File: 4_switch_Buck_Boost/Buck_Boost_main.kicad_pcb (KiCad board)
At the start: 4 copper layers, 95 parts, among them J1 Conn_02x02_Counter_Clockwise, J2 Screw_Terminal_2x5.08, J3 Screw_Terminal_2x2.54, J4 Screw_Terminal_2x5.08, Q101 2N7002K, Q102 NVMFS6H836NLT1G, Q103 BSS83P, Q104 BSC070N10LS5, Q105 BSC070N10LS5, Q106 BSC070N10LS5, Q107 BSC070N10LS5, U1 LT8390EUFD_PBF, U101 LTC4372CMS8-PBF

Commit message: Add LT8390EFE#PBF footprint
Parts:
- removed U1: LT8390EUFD_PBF, LT:QFN50P500X400X80-29N
- added U102: LT8390EFE_PBF, LT:05-08-1663_ADI, F.Cu at (144.7, 104.8)
- moved H2 45.8 mm to (207.2, 75.7)
- moved H3 43.9 mm to (87.0, 135.8)
- moved H4 42.6 mm to (201.1, 129.5)
- moved H1 37.8 mm to (87.8, 80.9)
- moved C8 8.31 mm to (152.8, 111.0)
- moved R118 6.16 mm to (134.6, 108.3)
- moved C9 4.58 mm to (136.7, 105.0)
- moved C103 1.86 mm to (145.5, 95.3)
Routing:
- net SW1: track 24.8 -> 6.03 mm
- net ENABLE: track 41.5 -> 24.7 mm
- net SW2: track 20.7 -> 7.21 mm
- net BG1_CTRL: track 11.6 -> 0.00 mm
- net EN/UVLO: track 11.6 -> 0.49 mm
- net Net-(U102-~{PGOOD}): track 9.25 -> 0.04 mm
- net TG1_CTRL: track 7.43 -> 0.00 mm
- net FB: track 25.9 -> 18.9 mm
- net TG2_CTRL: track 6.75 -> 0.00 mm
- net Vout: track 26.5 -> 19.8 mm
- net BG2_CTRL: track 6.33 -> 0.00 mm
- net /Vref: track 6.13 -> 0.00 mm
- net Net-(U102-RT): track 12.9 -> 7.66 mm
- net Net-(U102-SS): track 3.61 -> 0.00 mm
- net Net-(U102-VC): track 3.92 -> 0.52 mm
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
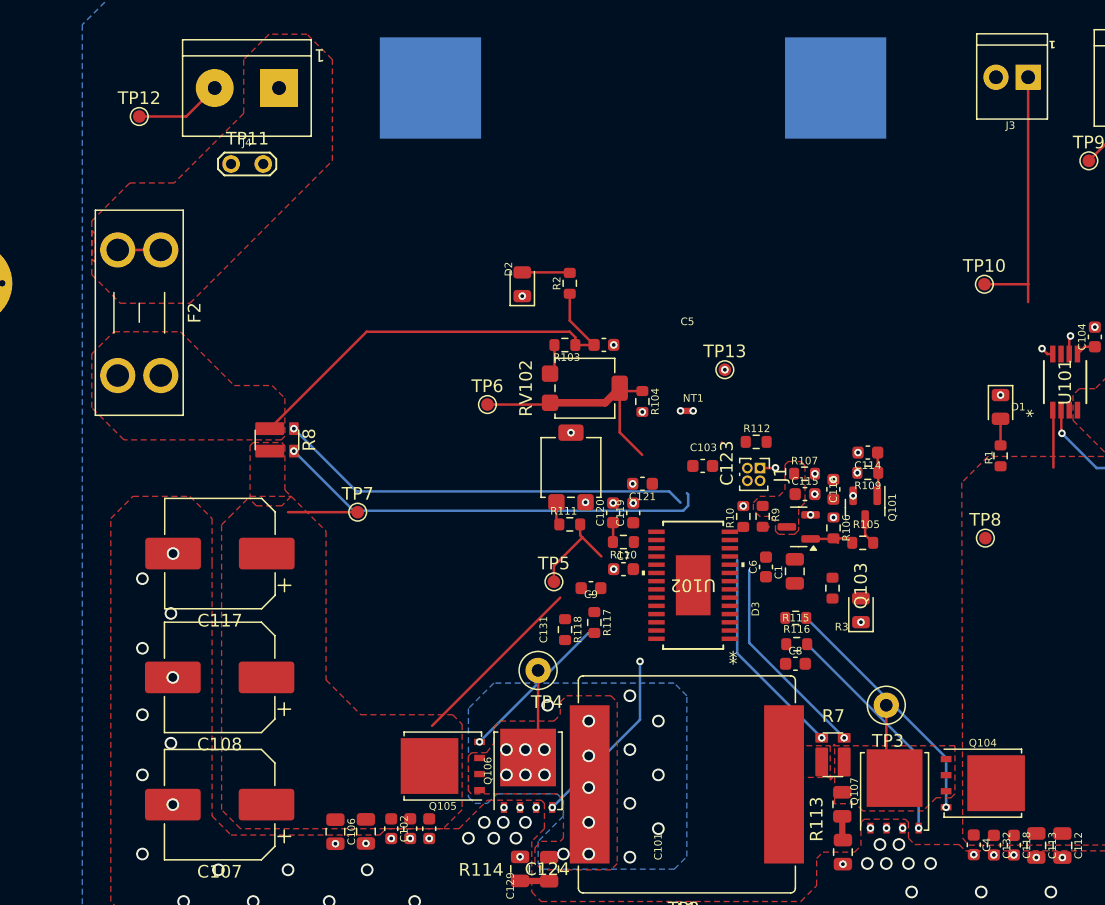
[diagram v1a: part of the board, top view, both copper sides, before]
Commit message: Reconfigured All Analog traces and GNDA island
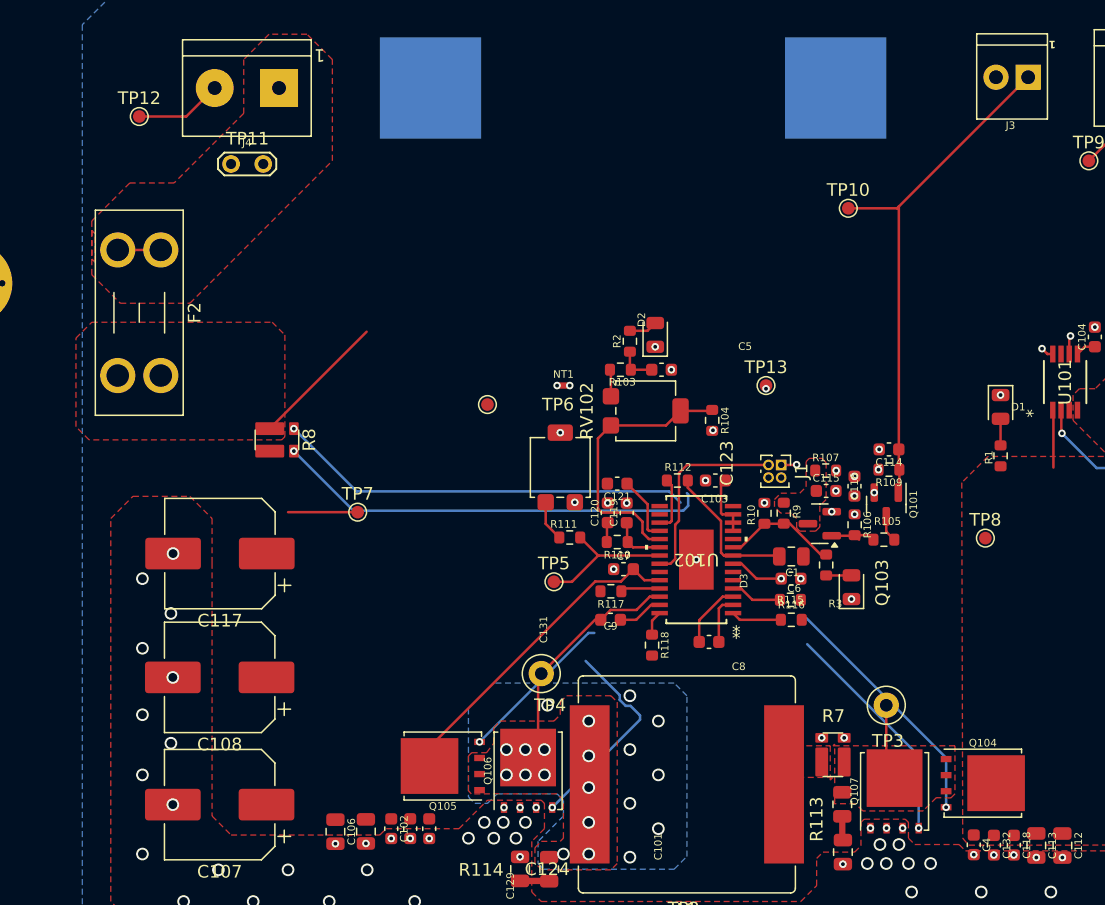
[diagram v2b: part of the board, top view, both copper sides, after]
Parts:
- moved TP10 12.3 mm to (157.0, 75.0)
- moved D2 11.2 mm to (141.8, 85.0)
- moved NT1 9.95 mm to (134.5, 89.0)
- moved C8 7.04 mm to (146.0, 109.2), turned to 180 degrees
- moved R118 6.98 mm to (141.5, 109.5)
- moved R112 6.93 mm to (143.5, 96.5)
- moved R2 6.59 mm to (139.8, 85.5)
- moved R104 5.71 mm to (146.2, 91.8)
- moved RV102 5.13 mm to (141.0, 91.0)
- moved C5 4.96 mm to (142.2, 87.8)
- moved R103 4.80 mm to (139.0, 87.8)
- moved TP13 3.48 mm to (150.5, 89.0)
- moved C9 2.94 mm to (138.2, 107.5)
- moved R117 2.79 mm to (138.2, 105.2), turned to 180 degrees
- moved C6 2.18 mm to (152.5, 104.2), turned to 180 degrees
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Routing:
- net Vout_FB: track 34.7 -> 14.2 mm
- net LSN: track 16.8 -> 0.00 mm
- net ENABLE: track 24.7 -> 41.1 mm
- net LSP: track 16.5 -> 0.15 mm
- net SYNC/SPRD: track 0.00 -> 15.6 mm
- net SW2: track 7.21 -> 19.4 mm
- net Vout: track 19.8 -> 31.4 mm
- net /INTVCC: track 0.00 -> 11.5 mm
- net EN/UVLO: track 0.49 -> 9.14 mm
- net Net-(U102-SS): track 0.00 -> 5.29 mm
- net SW1: track 6.03 -> 11.2 mm
- net /Vref: track 0.00 -> 5.00 mm
- net Net-(U102-~{PGOOD}): track 0.04 -> 4.36 mm
- net Vin: track 0.49 -> 4.78 mm, vias 2 -> 4
- net TG1_CTRL: track 0.00 -> 4.07 mm
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- removed copper zone on F.Cu, net Vout

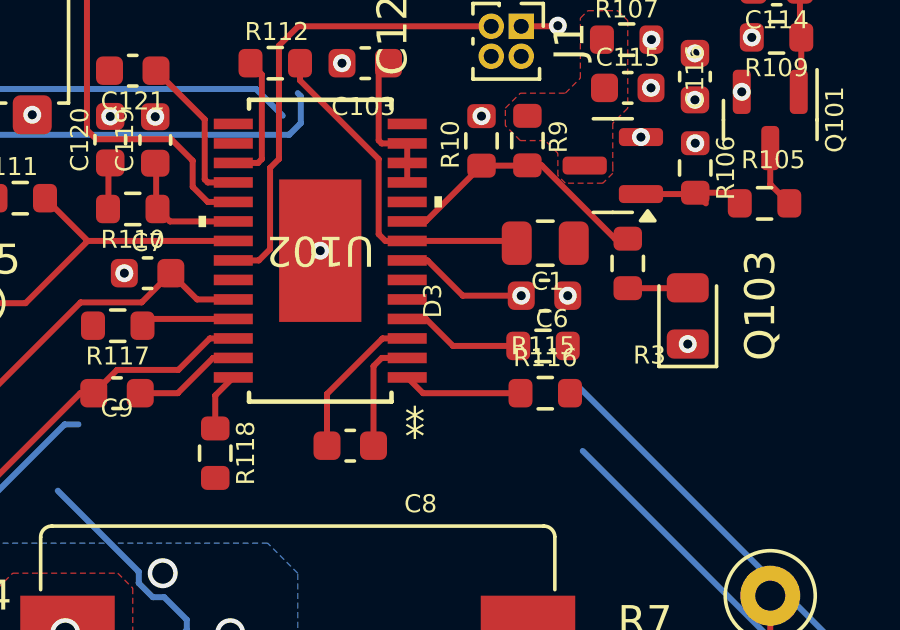
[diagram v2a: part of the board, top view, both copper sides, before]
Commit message: Reconfigured Analog traces and GNDA island
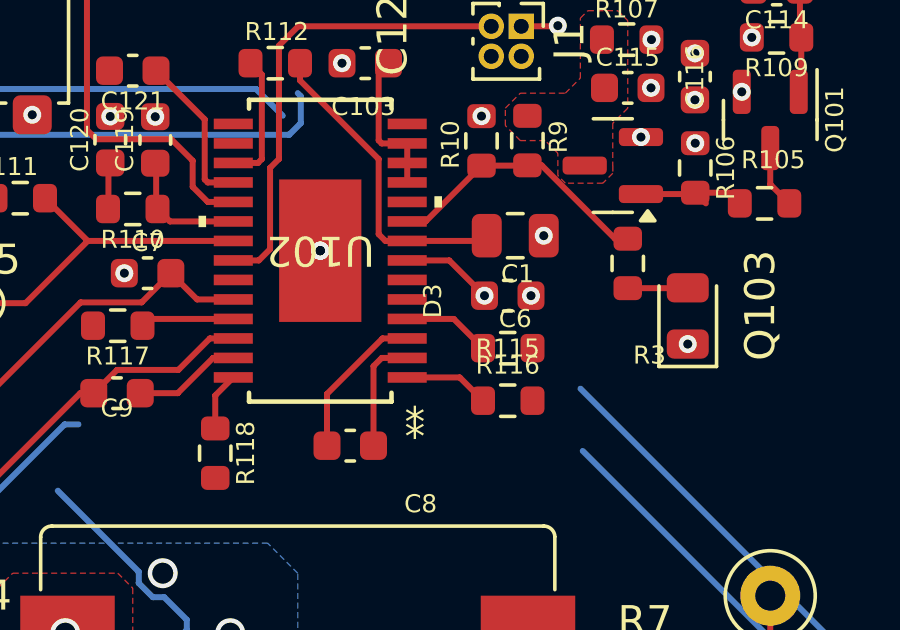
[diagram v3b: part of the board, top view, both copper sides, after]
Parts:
- moved R116 1.27 mm to (151.2, 107.8)
- moved C6 1.22 mm to (151.2, 104.2)
- moved R115 1.18 mm to (151.2, 106.0)
- moved C1 1.03 mm to (151.5, 102.2)
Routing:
- net Vin: track 4.78 -> 3.56 mm
- net BG1_CTRL: track 3.99 -> 2.85 mm
- net TG1_CTRL: track 4.07 -> 2.93 mm
- net /INTVCC: track 11.5 -> 10.6 mm
- net GNDA: vias 11 -> 12
- net GND: vias 93 -> 95
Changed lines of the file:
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@@
 	(footprint "rsx_capacitors:C_0603_1608Metric"
 		(layer "F.Cu")
-		(at 152.475 104.25 180)
+		(at 151.25 104.25 180)
 		(descr "Capacitor SMD 0603 (1608 Metric), square (rectangular) end terminal, IPC_7351 nominal, (Body size source: IPC-SM-782 page 76, https://www.pcb-3d.com/wordpress/wp-content/uploads/ipc-sm-782a_amendment_1_and_2.pdf), generated with kicad-footprint-generator")
 		(tags "capacitor")
@@
 	(footprint "rsx_capacitors:C_0805_2012Metric"
 		(layer "F.Cu")
-		(at 152.5 102.5 180)
+		(at 151.5 102.25 180)
 		(descr "Capacitor SMD 0805 (2012 Metric), square (rectangular) end terminal, IPC_7351 nominal, (Body size source: IPC-SM-782 page 76, https://www.pcb-3d.com/wordpress/wp-content/uploads/ipc-sm-782a_amendment_1_and_2.pdf, https://docs.google.com/spreadsheets/d/1BsfQQcO9C6DZCsRaXUlFlo91Tg2WpOkGARC1WS5S8t0/edit?usp=sharing), generated with kicad-footprint-generator")
 		(tags "capacitor")
@@
 	(footprint "rsx_resistors:R_0603_1608Metric"
 		(layer "F.Cu")
-		(at 152.5 107.5)
+		(at 151.25 107.75)
 		(descr "Resistor SMD 0603 (1608 Metric), square (rectangular) end terminal, IPC_7351 nominal, (Body size source: IPC-SM-782 page 72, https://www.pcb-3d.com/wordpress/wp-content/uploads/ipc-sm-782a_amendment_1_and_2.pdf), generated with kicad-footprint-generator")
 		(tags "resistor")
@@
 	(footprint "rsx_resistors:R_0603_1608Metric"
 		(layer "F.Cu")
-		(at 152.425 105.925)
+		(at 151.25 106)
 		(descr "Resistor SMD 0603 (1608 Metric), square (rectangular) end terminal, IPC_7351 nominal, (Body size source: IPC-SM-782 page 72, https://www.pcb-3d.com/wordpress/wp-content/uploads/ipc-sm-782a_amendment_1_and_2.pdf), generated with kicad-footprint-generator")
 		(tags "resistor")
@@
 	)
 	(via
+		(at 152.45 102.25)
+		(size 0.6)
+		(drill 0.3)
+		(layers "F.Cu" "B.Cu")
+		(net 1)
+	)
+	(via
 		(at 135.4 98.22)
 		(size 0.6)
@@
 	(segment
 		(start 147.899148 102.425007)
-		(end 151.475007 102.425007)
-		(width 0.2)
-		(layer "F.Cu")
-		(net 2)
-	)
-	(segment
-		(start 151.475007 102.425007)
-		(end 151.55 102.5)
+		(end 150.374993 102.425007)
 		(width 0.2)
 		(layer "F.Cu")
@@
 	)
 	(segment
+		(start 150.374993 102.425007)
+		(end 150.55 102.25)
+		(width 0.2)
+		(layer "F.Cu")
+		(net 2)
+	)
+	(segment
 		(start 178.965 68.285)
 		(end 176 71.25)
@@
 	)
 	(via
+		(at 145 102.75)
+		(size 0.6)
+		(drill 0.3)
+		(layers "F.Cu" "B.Cu")
+		(net 3)
+	)
+	(via
 		(at 116.4914 125.185)
 		(size 0.6)
@@
 	)
 	(via
-		(at 153.25 104.25)
+		(at 152.025 104.25)
 		(size 0.6)
 		(drill 0.3)
@@
 	)
 	(via
+		(at 145 102.75)
+		(size 0.6)
+		(drill 0.3)
+		(layers "F.Cu" "B.Cu")
+		(net 3)
+	)
+	(via
 		(at 172.300001 86.0845)
 		(size 0.6)
@@
 	(segment
 		(start 147.899148 103.074993)
-		(end 148.574993 103.074993)
+		(end 149.299993 103.074993)
 		(width 0.2)
 		(layer "F.Cu")
@@
 	)
 	(segment
-		(start 149.75 104.25)
-		(end 151.7 104.25)
-		(width 0.2)
-		(layer "F.Cu")
-		(net 4)
-	)
-	(segment
-		(start 148.574993 103.074993)
-		(end 149.75 104.25)
+		(start 149.299993 103.074993)
+		(end 150.475 104.25)
 		(width 0.2)
 		(layer "F.Cu")
@@
 	)
 	(via
-		(at 157.49 97.7225)
+		(at 150.475 104.25)
 		(size 0.6)
 		(drill 0.3)
@@
 	)
 	(via
-		(at 151.7 104.25)
+		(at 157.49 97.7225)
 		(size 0.6)
 		(drill 0.3)
@@
 	(segment
 		(start 147.899148 105.024951)
-		(end 148.524951 105.024951)
-		(width 0.2)
-		(layer "F.Cu")
-		(net 28)
-	)
-	(segment
-		(start 149.425 105.925)
-		(end 151.6 105.925)
+		(end 149.449951 105.024951)
 		(width 0.2)
 		(layer "F.Cu")
@@
 	)
 	(segment
-		(start 148.524951 105.024951)
-		(end 149.425 105.925)
+		(start 149.449951 105.024951)
+		(end 150.425 106)
 		(width 0.2)
 		(layer "F.Cu")
@@
 	)
 	(segment
-		(start 148.424239 107.5)
-		(end 151.675 107.5)
+		(start 147.899148 106.974909)
+		(end 149.649909 106.974909)
 		(width 0.2)
 		(layer "F.Cu")
@@
 	)
 	(segment
-		(start 147.899148 106.974909)
-		(end 148.424239 107.5)
+		(start 149.649909 106.974909)
+		(end 150.425 107.75)
 		(width 0.2)
 		(layer "F.Cu")
@@
 			)
 		)
+	)
+	(zone
+		(net 1)
+		(net_name "GNDA")
+		(layer "In1.Cu")
+		(hatch edge 0.5)
+		(priority 11)
+		(connect_pads
+			(clearance 0.5)
+		)
+		(min_thickness 0.25)
+		(filled_areas_thickness no)
+		(fill yes
+			(thermal_gap 0.5)
+			(thermal_bridge_width 0.5)
+		)
+		(polygon
+			(pts
+				(xy 146.75 103) (xy 147 103.25) (xy 153.75 103.25) (xy 154.25 102.75) (xy 154.25 99.75) (xy 147.5 99.75)
+				(xy 146.75 100.5)
+			)
+		)

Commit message: Adding DPN - not done yet
clean stuff and some dpn

cleanup AND moar dpn

more cleanup
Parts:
- C104: value 100n -> 0.1u
- J1: footprint Connector_PinHeader_1.00mm:PinHeader_2x02_P1.00mm_Vertical -> Connector_PinHeader_2.54mm:PinHeader_2x02_P2.54mm_Vertical
- R105, R106, R107, R109: value 100K -> 100k
- R113, R114: footprint Capacitor_SMD:C_0805_2012Metric -> rsx_resistors:R_0603_1608Metric
- TP3, TP4: footprint TestPoint:TestPoint_Loop_D1.80mm_Drill1.0mm_Beaded -> TestPoint:TestPoint_Loop_D2.50mm_Drill1.0mm_LowProfile

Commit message: finish analog connections change rsense footprint
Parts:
- R7: footprint Littelfuse_L4CA0612_KiCad9:Littelfuse_L4CA0612_4Terminal -> WLTM:WLTM0612_R002-R100_Kelvin
- moved C104 17.1 mm to (191.7, 92.8)
- moved U101 15.3 mm to (188.9, 92.6), turned to -90 degrees
- moved D3 11.0 mm to (164.8, 96.9), turned to -90 degrees
- moved R3 9.75 mm to (164.8, 101.0), turned to 90 degrees
- moved C1 8.55 mm to (146.0, 95.7), turned to -90 degrees
- moved C103 7.63 mm to (154.1, 97.1), turned to -90 degrees
- moved C6 6.53 mm to (157.8, 104.1), turned to 90 degrees
- moved C7 5.41 mm to (134.2, 105.5), turned to 90 degrees
- moved C9 4.37 mm to (142.1, 109.5), turned to -90 degrees
- moved TP4 2.92 mm to (129.9, 111.0)
- moved TP3 2.53 mm to (161.2, 112.0)
- moved C5 2.51 mm to (142.0, 85.2)
- moved D2 2.51 mm to (141.5, 82.5)
- moved R103 2.51 mm to (138.8, 85.2)
- moved R104 2.51 mm to (146.0, 89.2)
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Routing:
- net Vin: track 3.56 -> 30.7 mm, vias 4 -> 3
- net LSP: track 0.15 -> 20.5 mm, vias 1 -> 2
- net Vout_FB: track 14.2 -> 34.0 mm
- net ENABLE: track 41.1 -> 22.0 mm
- net LSN: track 0.00 -> 18.9 mm, vias 1 -> 0
- net Vout: track 31.4 -> 15.0 mm
- net ISN: track 33.0 -> 42.0 mm, vias 1 -> 2
- net EN/UVLO: track 9.14 -> 17.1 mm
- net ISP: track 34.3 -> 41.7 mm, vias 1 -> 2
- net Net-(Q102-G): track 12.2 -> 6.88 mm, vias 2 -> 0
- net SYNC/SPRD: track 15.6 -> 20.3 mm
- net SW2: track 19.4 -> 15.4 mm, vias 20 -> 1
- net SW1: track 11.2 -> 15.0 mm
- net Net-(Q102-D): track 4.43 -> 7.71 mm
- net Net-(U101-INTVCC): track 1.61 -> 4.83 mm
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- removed copper zone on In1.Cu, net GNDA
- removed copper zone on B.Cu, net SW2
- removed copper zone on In2.Cu, net SW2
